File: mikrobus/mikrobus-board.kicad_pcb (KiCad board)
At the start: 2 copper layers, 67.3 x 64.8 mm, 9 parts, among them J1 Conn_01x06, P3 microBus_1, P4 microBus_2, P5 microBus_1, P6 microBus_2

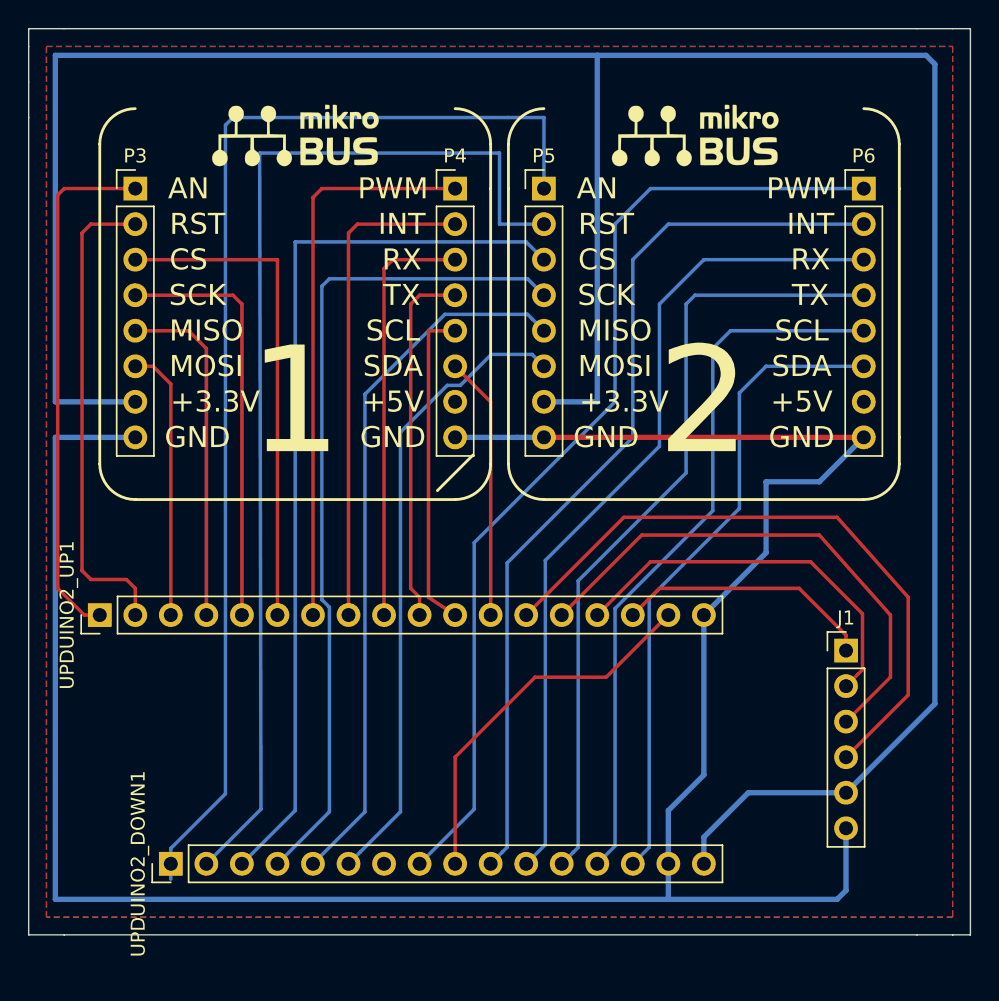
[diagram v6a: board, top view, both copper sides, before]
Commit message: Fixed silk
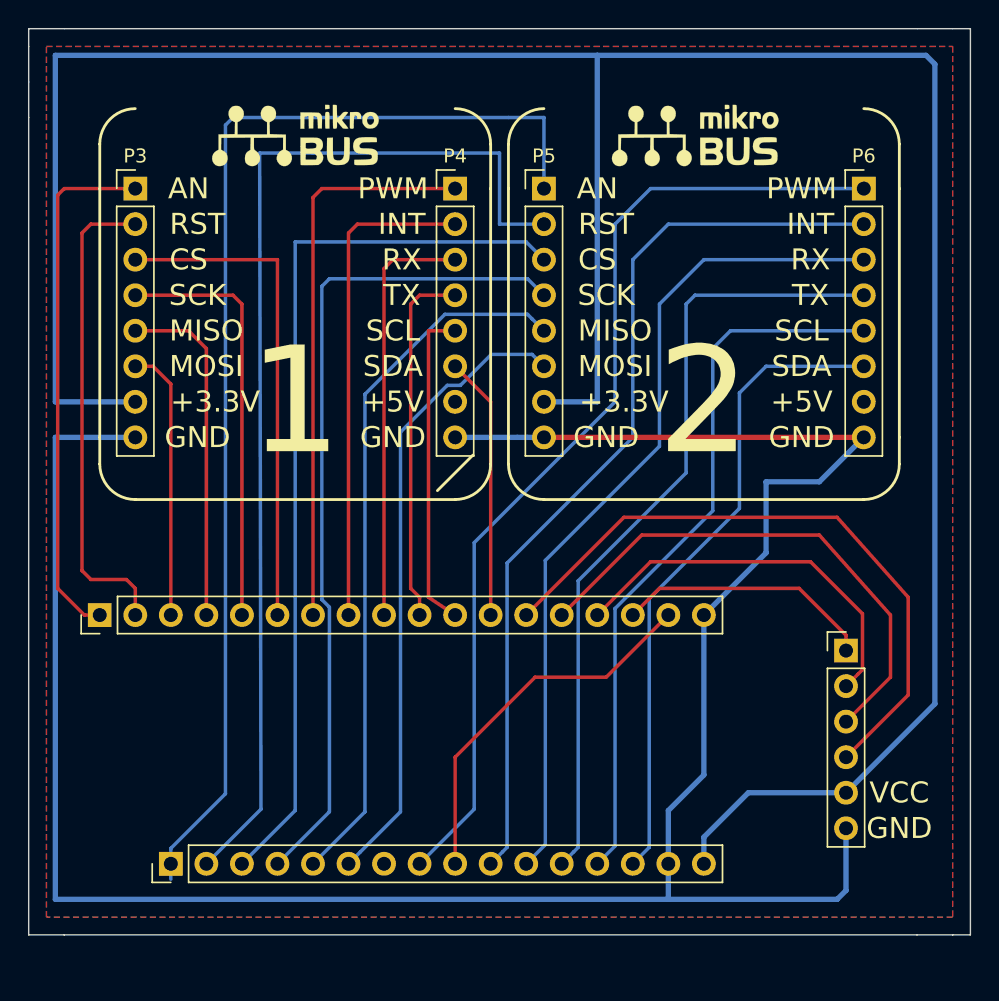
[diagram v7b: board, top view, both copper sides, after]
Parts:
- renumbered UPDUINO2_UP1 to UP1
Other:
- board text added: "VCC"
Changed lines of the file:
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@@
     (area 116.789999 100.279999 184.200001 165.150001)
     (thickness 1.6)
-    (drawings 70)
+    (drawings 72)
     (tracks 176)
     (zones 0)
@@
     (36 B.SilkS user)
     (37 F.SilkS user)
-    (38 B.Mask user)
-    (39 F.Mask user)
-    (40 Dwgs.User user)
-    (41 Cmts.User user)
-    (42 Eco1.User user)
-    (43 Eco2.User user)
-    (44 Edge.Cuts user)
-    (45 Margin user)
-    (46 B.CrtYd user)
-    (47 F.CrtYd user)
-    (48 B.Fab user)
-    (49 F.Fab user)
+    (38 B.Mask user hide)
+    (39 F.Mask user hide)
+    (40 Dwgs.User user hide)
+    (41 Cmts.User user hide)
+    (42 Eco1.User user hide)
+    (43 Eco2.User user hide)
+    (44 Edge.Cuts user hide)
+    (45 Margin user hide)
+    (46 B.CrtYd user hide)
+    (47 F.CrtYd user hide)
+    (48 B.Fab user hide)
+    (49 F.Fab user hide)
   )
   (setup
@@
     (descr "Through hole straight socket strip, 1x18, 2.54mm pitch, single row")
     (tags "Through hole socket strip THT 1x18 2.54mm single row")
-    (fp_text reference UPDUINO2_UP1 (at 0 -2.33 90) (layer F.SilkS)
+    (fp_text reference UP1 (at 0 -2.33 90) (layer F.SilkS) hide
       (effects (font (size 1 1) (thickness 0.15)))
     )
@@
     (descr "Through hole straight pin header, 1x06, 2.54mm pitch, single row")
     (tags "Through hole pin header THT 1x06 2.54mm single row")
-    (fp_text reference J1 (at 0 -2.33) (layer F.SilkS)
+    (fp_text reference J1 (at 0 -2.33) (layer F.SilkS) hide
       (effects (font (size 1 1) (thickness 0.15)))
     )
@@
     (descr "Through hole straight socket strip, 1x16, 2.54mm pitch, single row")
     (tags "Through hole socket strip THT 1x16 2.54mm single row")
-    (fp_text reference UPDUINO2_DOWN1 (at 0 -2.33 90) (layer F.SilkS)
+    (fp_text reference UPDUINO2_DOWN1 (at 0 -2.33 90) (layer F.SilkS) hide
       (effects (font (size 1 1) (thickness 0.15)))
     )
@@
       (xy 2.292195 -2.172368) (xy 2.384376 -2.169505)) (layer F.SilkS) (width 0.01))
   )
+  (gr_text GND (at 179.07 157.48) (layer F.SilkS)
+    (effects (font (size 1.5 1.5) (thickness 0.3)))
+  )
+  (gr_text VCC (at 179.07 154.94) (layer F.SilkS)
+    (effects (font (size 1.5 1.5) (thickness 0.3)))
+  )
   (gr_line (start 184.15 100.33) (end 184.15 165.1) (angle 90) (layer Edge.Cuts) (width 0.1))
